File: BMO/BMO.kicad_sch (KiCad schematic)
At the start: 0 parts

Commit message: update pcb
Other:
- added sheet Sensors (Sensors.kicad_sch)
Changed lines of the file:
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@@
+		)
+	)
+	(sheet
+		(at 154.94 46.99)
+		(size 44.45 64.77)
+		(exclude_from_sim no)
+		(in_bom yes)
+		(on_board yes)
+		(dnp no)
+		(fields_autoplaced yes)
+		(stroke
+			(width 0.1524)
+			(type solid)
+		)
+		(fill
+			(color 0 0 0 0)
+		)
+		(property "Sheetname" "Sensors"
+			(at 154.94 46.2784 0)
+			(show_name no)
+			(do_not_autoplace no)
+			(effects
+				(font
+					(size 1.27 1.27)
+				)
+				(justify left bottom)
+			)
+		)
+		(property "Sheetfile" "Sensors.kicad_sch"
+			(at 154.94 112.3446 0)
+			(show_name no)
+			(do_not_autoplace no)
+			(effects
+				(font
+					(size 1.27 1.27)
+				)
+				(justify left top)
+			)
+		)
+		(instances
+			(project "BMO"
+				(path "/509804e7-65e7-46e6-80ed-6cdb4037dc07"
+					(page "3")
+				)
+			)
 		)
 	)

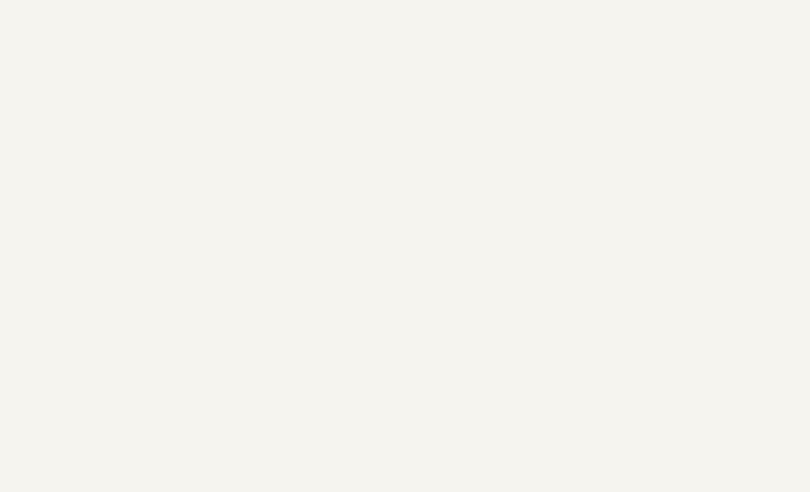
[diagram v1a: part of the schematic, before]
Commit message: Update KiCad files, add Power schematic
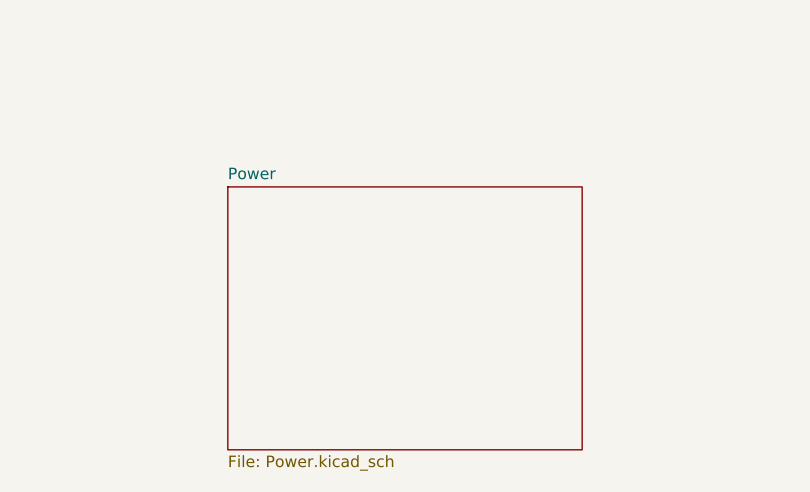
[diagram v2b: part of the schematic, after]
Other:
- added sheet Power (Power.kicad_sch)
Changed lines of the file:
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@@
+	)
+	(sheet
+		(at 104.14 148.59)
+		(size 39.37 29.21)
+		(exclude_from_sim no)
+		(in_bom yes)
+		(on_board yes)
+		(dnp no)
+		(fields_autoplaced yes)
+		(stroke
+			(width 0.1524)
+			(type solid)
+		)
+		(fill
+			(color 0 0 0 0)
+		)
+		(property "Sheetname" "Power"
+			(at 104.14 147.8784 0)
+			(show_name no)
+			(do_not_autoplace no)
+			(effects
+				(font
+					(size 1.27 1.27)
+				)
+				(justify left bottom)
+			)
+		)
+		(property "Sheetfile" "Power.kicad_sch"
+			(at 104.14 178.3846 0)
+			(show_name no)
+			(do_not_autoplace no)
+			(effects
+				(font
+					(size 1.27 1.27)
+				)
+				(justify left top)
+			)
+		)
+		(instances
+			(project "BMO"
+				(path "/509804e7-65e7-46e6-80ed-6cdb4037dc07"
+					(page "4")
+				)
+			)
+		)
 	)
 	(sheet

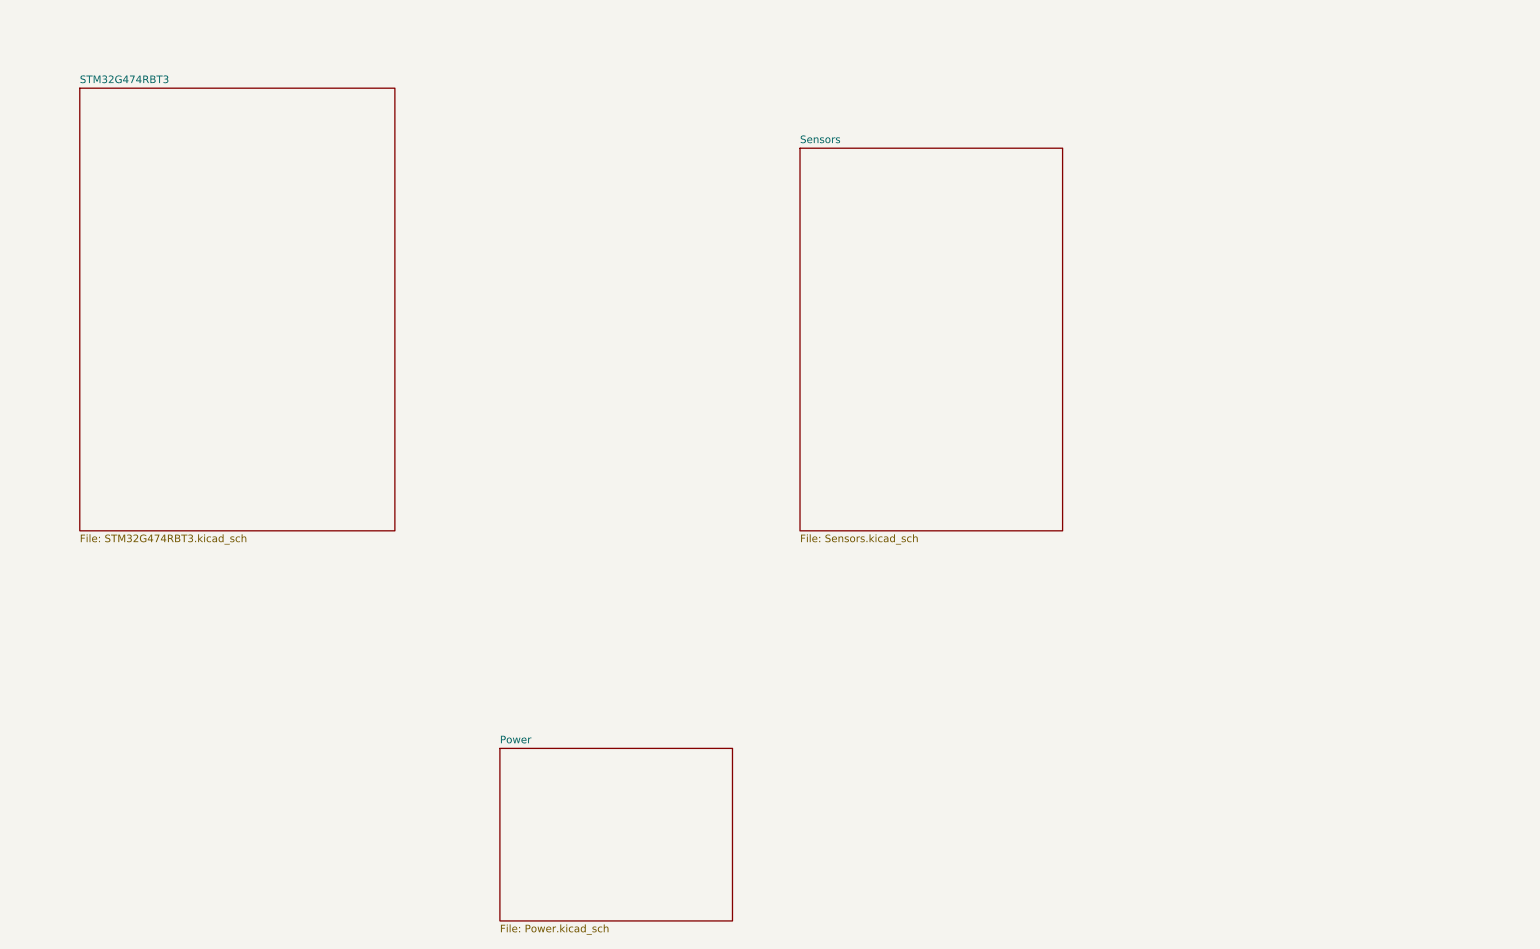
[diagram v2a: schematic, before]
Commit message: Updated Power schematic, Added Motors driver schematic
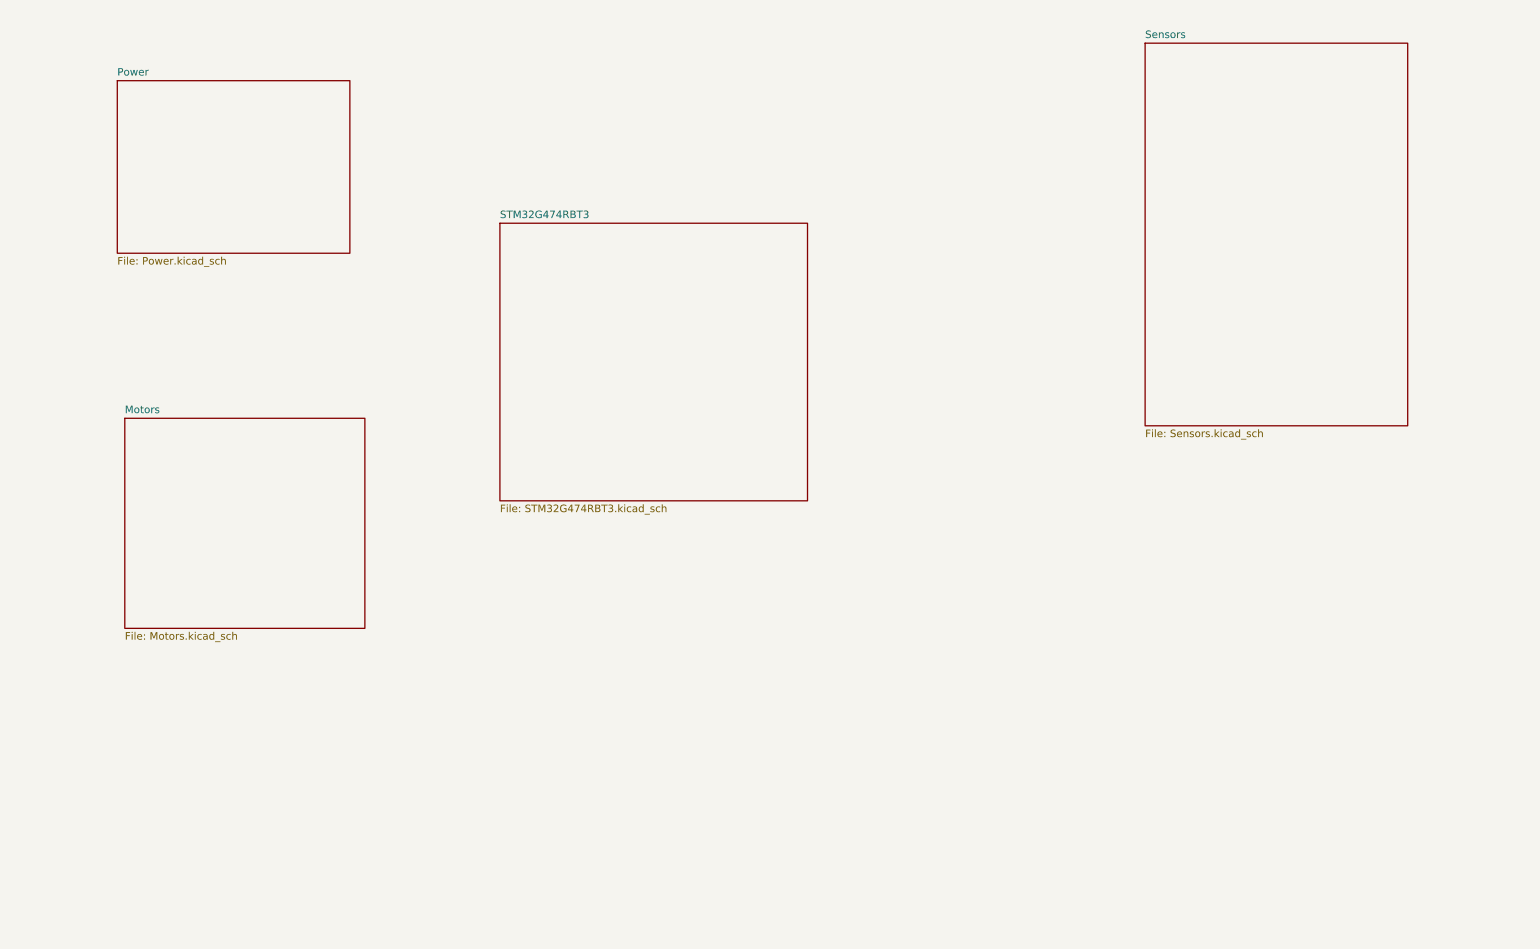
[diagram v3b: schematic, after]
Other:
- added sheet Motors (Motors.kicad_sch)
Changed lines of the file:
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@@
 	)
 	(sheet
-		(at 33.02 36.83)
-		(size 53.34 74.93)
+		(at 104.14 59.69)
+		(size 52.07 46.99)
 		(exclude_from_sim no)
 		(in_bom yes)
@@
 		)
 		(property "Sheetname" "STM32G474RBT3"
-			(at 33.02 36.1184 0)
+			(at 104.14 58.9784 0)
 			(show_name no)
 			(do_not_autoplace no)
@@
 		)
 		(property "Sheetfile" "STM32G474RBT3.kicad_sch"
-			(at 33.02 112.3446 0)
+			(at 104.14 107.2646 0)
 			(show_name no)
 			(do_not_autoplace no)
@@
 	)
 	(sheet
-		(at 104.14 148.59)
+		(at 40.64 92.71)
+		(size 40.64 35.56)
+		(exclude_from_sim no)
+		(in_bom yes)
+		(on_board yes)
+		(dnp no)
+		(fields_autoplaced yes)
+		(stroke
+			(width 0.1524)
+			(type solid)
+		)
+		(fill
+			(color 0 0 0 0)
+		)
+		(property "Sheetname" "Motors"
+			(at 40.64 91.9984 0)
+			(show_name no)
+			(do_not_autoplace no)
+			(effects
+				(font
+					(size 1.27 1.27)
+				)
+				(justify left bottom)
+			)
+		)
+		(property "Sheetfile" "Motors.kicad_sch"
+			(at 40.64 128.8546 0)
+			(show_name no)
+			(do_not_autoplace no)
+			(effects
+				(font
+					(size 1.27 1.27)
+				)
+				(justify left top)
+			)
+		)
+		(instances
+			(project "BMO"
+				(path "/509804e7-65e7-46e6-80ed-6cdb4037dc07"
+					(page "5")
+				)
+			)
+		)
+	)
+	(sheet
+		(at 39.37 35.56)
 		(size 39.37 29.21)
 		(exclude_from_sim no)
@@
 		)
 		(property "Sheetname" "Power"
-			(at 104.14 147.8784 0)
+			(at 39.37 34.8484 0)
 			(show_name no)
 			(do_not_autoplace no)
@@
 		)
 		(property "Sheetfile" "Power.kicad_sch"
-			(at 104.14 178.3846 0)
+			(at 39.37 65.3546 0)
 			(show_name no)
 			(do_not_autoplace no)
@@
 	)
 	(sheet
-		(at 154.94 46.99)
+		(at 213.36 29.21)
 		(size 44.45 64.77)
 		(exclude_from_sim no)
@@
 		)
 		(property "Sheetname" "Sensors"
-			(at 154.94 46.2784 0)
+			(at 213.36 28.4984 0)
 			(show_name no)
 			(do_not_autoplace no)
@@
 		)
 		(property "Sheetfile" "Sensors.kicad_sch"
-			(at 154.94 112.3446 0)
+			(at 213.36 94.5646 0)
 			(show_name no)
 			(do_not_autoplace no)

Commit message: Update sensor and MCU files
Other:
- sheet Motors ports: added ENC_L_A_TIM2_CH1, ENC_L_B_TIM2_CH2, ENC_R_A_TIM4_CH1, ENC_R_B_TIM4_CH2, MOT_L_IN1_TIM3_CH1, MOT_L_IN2_TIM3_CH2, MOT_R_IN1_TIM3_CH3, MOT_R_IN2_TIM3_CH4, SERVO_PINCE_TIM8_CH1; removed none
- sheet Power ports: added Boost_EN, CHRG_OTG, I2C1_SCL_MPU-6050 & Jauge, I2C1_SDA_MPU-6050 & Jauge, linear_regulator_EN; removed none
- sheet STM32G474RBT3 ports: added BLE_USART3_RX, BLE_USART3_TX, ENC_L_A_TIM2_CH1, ENC_L_B_TIM2_CH2, ENC_R_A_TIM4_CH1, ENC_R_B_TIM4_CH2, I2C1_SCL_MPU-6050 & Jauge, I2C1_SDA_MPU-6050 & Jauge, I2C2_SCL_OLED, I2C2_SDA_OLED, I2C3_SCL_ToF_TCS, I2C3_SDA_ToF_TCS, LIDARX2__USART1_RX, LIDAR_M_CTR_TIM15_CH1, MOT_L_IN1_TIM3_CH1, MOT_L_IN2_TIM3_CH2, MOT_R_IN1_TIM3_CH3, MOT_R_IN2_TIM3_CH4, SERVO_PINCE_TIM8_CH1, XSHUT_TOF1, XSHUT_TOF2; removed none
- sheet Sensors ports: added BLE_En, BLE_USART3_RX, BLE_USART3_TX, I2C2_SCL_OLED, I2C2_SDA_OLED, I2C3_SCL_ToF_TCS, I2C3_SDA_ToF_TCS, LIDARX2__USART1_RX, LIDAR_M_CTR_TIM15_CH1, ToF1_Pin, ToF2_Pin, XSHUT_TOF1, XSHUT_TOF2; removed none

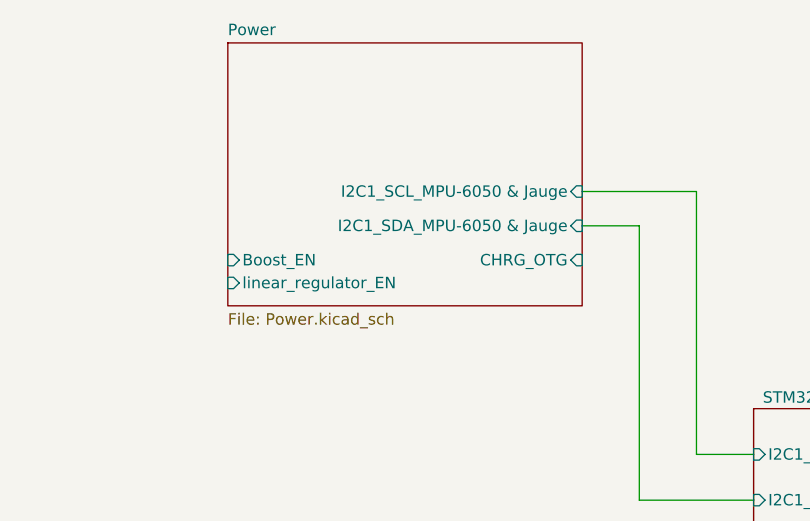
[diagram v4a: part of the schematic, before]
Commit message: changed the charger to BQ25896RTW and updated the shematic
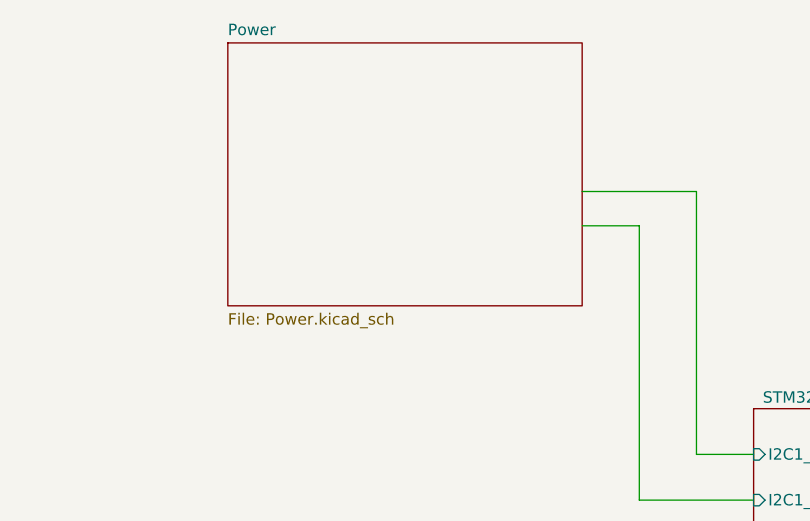
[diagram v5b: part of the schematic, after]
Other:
- sheet Power ports: added none; removed Boost_EN, CHRG_OTG, I2C1_SCL_MPU-6050 & Jauge, I2C1_SDA_MPU-6050 & Jauge, linear_regulator_EN
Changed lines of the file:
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@@
-			)
-		)
-		(pin "I2C1_SCL_MPU-6050 & Jauge" input
-			(at 92.71 43.18 0)
-			(effects
-				(font
-					(size 1.27 1.27)
-				)
-				(justify right)
-			)
-		)
-		(pin "I2C1_SDA_MPU-6050 & Jauge" input
-			(at 92.71 46.99 0)
-			(effects
-				(font
-					(size 1.27 1.27)
-				)
-				(justify right)
-			)
-		)
-		(pin "CHRG_OTG" input
-			(at 92.71 50.8 0)
-			(effects
-				(font
-					(size 1.27 1.27)
-				)
-				(justify right)
-			)
-		)
-		(pin "Boost_EN" input
-			(at 53.34 50.8 180)
-			(effects
-				(font
-					(size 1.27 1.27)
-				)
-				(justify left)
-			)
-		)
-		(pin "linear_regulator_EN" input
-			(at 53.34 53.34 180)
-			(effects
-				(font
-					(size 1.27 1.27)
-				)
-				(justify left)
 			)
 		)

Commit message: Update PCB modifications
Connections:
- no-connect marks 0 -> 1
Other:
- sheet Motors ports: added ~{FAULT}, ~{SLEEP}; removed none
- sheet Power ports: added CHARGER_INT, CHARG_SCL, CHARG_SDA, FG_GPOUT, linear_regulator_EN, nQON; removed none
- sheet STM32G474RBT3 ports: added BLE_En, CHARGER_INT, COLOR_INT, FG_GPOUT, I2C1_SCL_ Jauge, I2C1_SDA_ Jauge, I2C3_SCL_ToF_TCS_MPU, I2C3_SDA_ToF_TCS_MPU, LIDAR_M_CTR_TIM16_CH1, MOT_nFAULT, MOT_nSLEEP, MPU_INT, TOF1_INT, TOF2_INT; removed I2C1_SCL_MPU-6050 & Jauge, I2C1_SDA_MPU-6050 & Jauge, I2C3_SCL_ToF_TCS, I2C3_SDA_ToF_TCS, LIDAR_M_CTR_TIM15_CH1
- sheet Sensors ports: added COLOR_INT, I2C3_SCL_ToF_TCS_MPU, I2C3_SDA_ToF_TCS_MPU, LIDAR_M_CTR_TIM16_CH1, MPU_INT; removed I2C3_SCL_ToF_TCS, I2C3_SDA_ToF_TCS, LIDAR_M_CTR_TIM15_CH1

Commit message: Schéma prêt pour le PCB
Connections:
- no-connect marks 1 -> 0
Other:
- sheet Power ports: added PWR_Bouton; removed nQON
- sheet STM32G474RBT3 ports: added I2C1_SCL_Jauge, I2C1_SDA_Jauge, NEOPIXEL, PWR_Bouton; removed I2C1_SCL_ Jauge, I2C1_SDA_ Jauge
- sheet Sensors ports: added NEOPIXEL, TOF1_INT, TOF2_INT; removed ToF1_Pin, ToF2_Pin
